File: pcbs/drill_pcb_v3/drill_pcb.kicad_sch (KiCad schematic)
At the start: 44 parts, among them J1 24V IN, J10 LIMIT SWITCH BOTTOM, J11 DEEP WEIGHT SENSOR, J12 SURFACE WEIGHT SENSOR, J13 SERVO 1, J14 SERVO 2, J15 STEPPER STORAGE, J16 TEST PADS, J2 uC COMMUNICATION, J3 ENCODER VERTICAL DRIVE, J4 LIMIT SWITCH TOP, J5 HEIGHT SENSOR, J6 STEPPER VERTICAL DRIVE, J7 DC MOTOR 24 V, J8 DC MOTOR UART, J9 ENCODER STORAGE, Q3 SI2333-TP, U1 ESP32-DevKitC, U2 LM3940, U3 INA219BxD

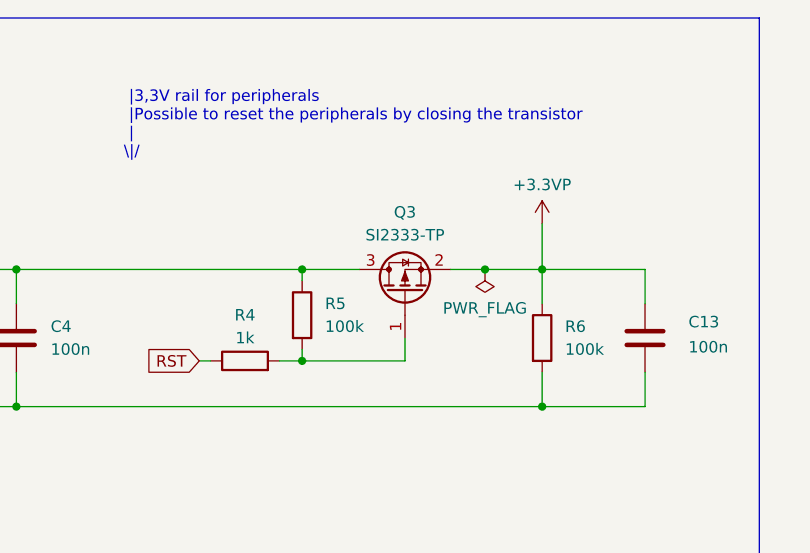
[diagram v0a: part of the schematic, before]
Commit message: Resolved mosfet misplacement for board v3. Deleted history.
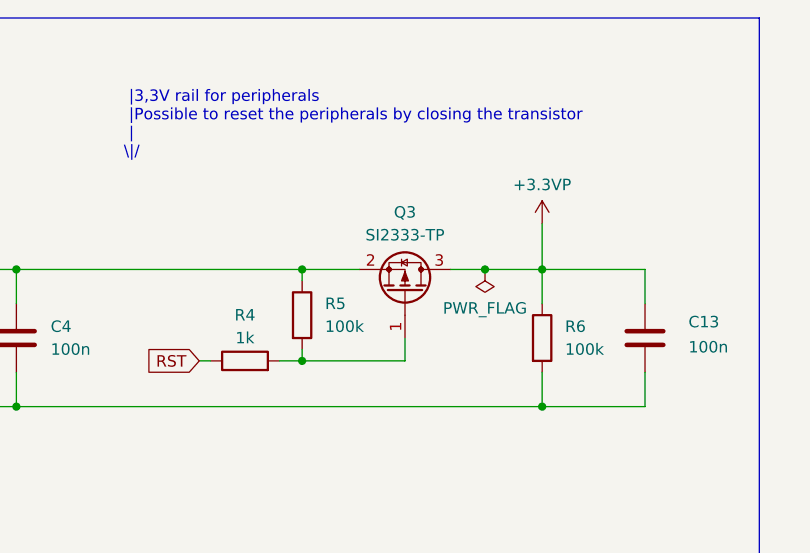
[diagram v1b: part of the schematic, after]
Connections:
- net +3.3V: now also Q3.2 (S); no longer Q3.3 (D)
- net +3.3VP: now also Q3.3 (D); no longer Q3.2 (S)
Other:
- moved on the sheet: Q3
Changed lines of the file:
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@@
 	)
 	(junction
-		(at 189.23 43.18)
-		(diameter 0)
-		(color 0 0 0 0)
-	)
-	(junction
 		(at 245.11 48.26)
 		(diameter 0)
@@
 	)
 	(junction
+		(at 189.23 43.18)
+		(diameter 0)
+		(color 0 0 0 0)
+	)
+	(junction
 		(at 231.14 116.84)
 		(diameter 0)
@@
 	)
 	(junction
-		(at 168.91 43.18)
+		(at 137.16 43.18)
 		(diameter 0)
 		(color 0 0 0 0)
 	)
 	(junction
-		(at 137.16 43.18)
+		(at 124.46 43.18)
 		(diameter 0)
 		(color 0 0 0 0)
 	)
 	(junction
-		(at 124.46 43.18)
+		(at 168.91 43.18)
 		(diameter 0)
 		(color 0 0 0 0)
@@
 	(symbol
 		(lib_id "Transistor_FET:Q_PMOS_GSD")
-		(at 180.34 45.72 90)
+		(at 180.34 45.72 270)
+		(mirror x)
 		(unit 1)
 		(body_style 1)
@@
 		(in_pos_files yes)
 		(dnp no)
-		(fields_autoplaced yes)
 		(property "Reference" "Q3"
 			(at 180.34 36.83 90)
@@
 		)
 		(property "Footprint" "Package_TO_SOT_SMD:SOT-23-3"
-			(at 177.8 40.64 0)
+			(at 182.88 40.64 0)
 			(hide yes)
 			(show_name no)

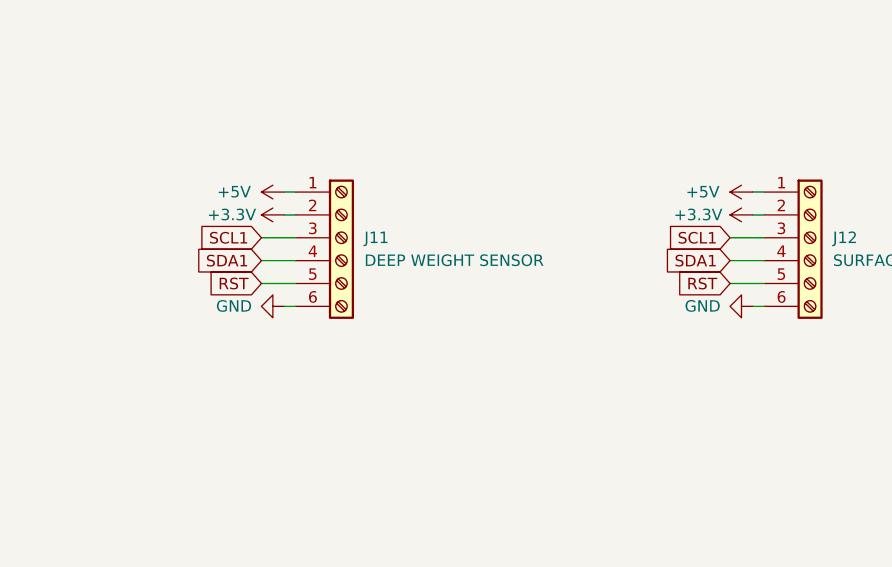
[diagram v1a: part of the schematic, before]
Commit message: ADC reset and Servo labels updated
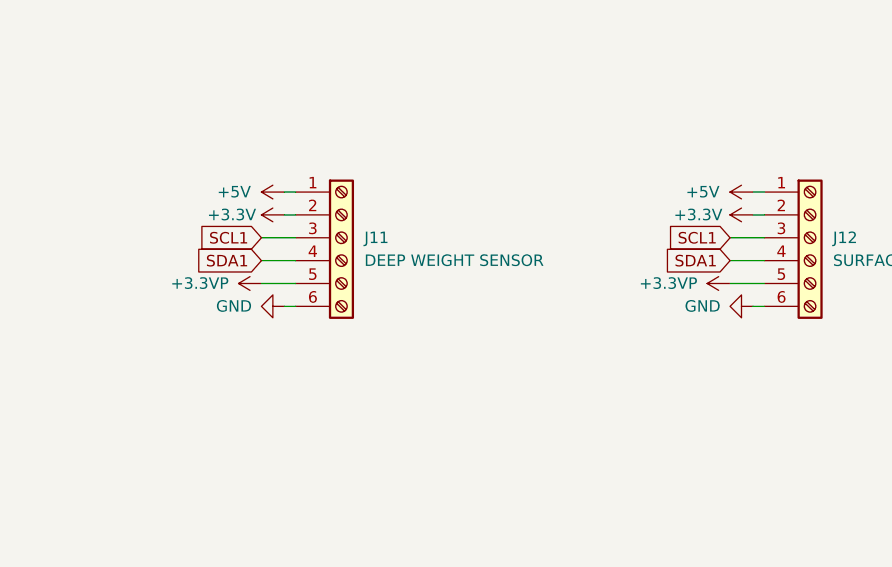
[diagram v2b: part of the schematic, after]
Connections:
- net +3.3VP: now also J11.5 (Pin_5), J12.5 (Pin_5)
- net RST: no longer J11.5 (Pin_5), J12.5 (Pin_5)
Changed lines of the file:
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@@
 		)
 	)
-	(global_label "RST"
-		(shape input)
-		(at 308.61 68.58 180)
-		(fields_autoplaced yes)
-		(effects
-			(font
-				(size 1.27 1.27)
-			)
-			(justify right)
-		)
-		(property "Intersheetrefs" "${INTERSHEET_REFS}"
-			(at 302.1777 68.58 0)
-			(hide yes)
-			(show_name no)
-			(do_not_autoplace no)
-			(effects
-				(font
-					(size 1.27 1.27)
-				)
-				(justify right)
-			)
-		)
-	)
 	(global_label "RX0"
 		(shape input)
@@
 		)
 	)
-	(global_label "RST"
-		(shape input)
-		(at 360.68 68.58 180)
-		(fields_autoplaced yes)
-		(effects
-			(font
-				(size 1.27 1.27)
-			)
-			(justify right)
-		)
-		(property "Intersheetrefs" "${INTERSHEET_REFS}"
-			(at 354.2477 68.58 0)
-			(hide yes)
-			(show_name no)
-			(do_not_autoplace no)
-			(effects
-				(font
-					(size 1.27 1.27)
-				)
-				(justify right)
-			)
-		)
-	)
 	(global_label "TX2"
 		(shape input)
@@
 	)
 	(symbol
+		(lib_id "power:+3.3VP")
+		(at 360.68 68.58 90)
+		(unit 1)
+		(body_style 1)
+		(exclude_from_sim no)
+		(in_bom yes)
+		(on_board yes)
+		(in_pos_files yes)
+		(dnp no)
+		(property "Reference" "#PWR045"
+			(at 361.95 64.77 0)
+			(hide yes)
+			(show_name no)
+			(do_not_autoplace no)
+			(effects
+				(font
+					(size 1.27 1.27)
+				)
+			)
+		)
+		(property "Value" "+3.3VP"
+			(at 353.822 68.58 90)
+			(show_name no)
+			(do_not_autoplace no)
+			(effects
+				(font
+					(size 1.27 1.27)
+				)
+			)
+		)
+		(property "Footprint" ""
+			(at 360.68 68.58 0)
+			(hide yes)
+			(show_name no)
+			(do_not_autoplace no)
+			(effects
+				(font
+					(size 1.27 1.27)
+				)
+			)
+		)
+		(property "Datasheet" ""
+			(at 360.68 68.58 0)
+			(hide yes)
+			(show_name no)
+			(do_not_autoplace no)
+			(effects
+				(font
+					(size 1.27 1.27)
+				)
+			)
+		)
+		(property "Description" "Power symbol creates a global label with name \"+3.3VP\""
+			(at 360.68 68.58 0)
+			(hide yes)
+			(show_name no)
+			(do_not_autoplace no)
+			(effects
+				(font
+					(size 1.27 1.27)
+				)
+			)
+		)
+		(pin "1"
+		)
+		(instances
+			(project "drill_pcb"
+				(path "/bebf97b1-2f7f-4d03-a427-fe976f4b2313"
+					(reference "#PWR045")
+					(unit 1)
+				)
+			)
+		)
+	)
+	(symbol
 		(lib_id "Device:R")
 		(at 168.91 48.26 0)
@@
 					(unit 1)
 				)
+			)
+		)
+	)
+	(symbol
+		(lib_id "power:+3.3VP")
+		(at 308.61 68.58 90)
+		(unit 1)
+		(body_style 1)
+		(exclude_from_sim no)
+		(in_bom yes)
+		(on_board yes)
+		(in_pos_files yes)
+		(dnp no)
+		(property "Reference" "#PWR044"
+			(at 309.88 64.77 0)
+			(hide yes)
+			(show_name no)
+			(do_not_autoplace no)
+			(effects
+				(font
+					(size 1.27 1.27)
+				)
+			)
+		)
+		(property "Value" "+3.3VP"
+			(at 301.752 68.58 90)
+			(show_name no)
+			(do_not_autoplace no)
+			(effects
+				(font
+					(size 1.27 1.27)
+				)
+			)
+		)
+		(property "Footprint" ""
+			(at 308.61 68.58 0)
+			(hide yes)
+			(show_name no)
+			(do_not_autoplace no)
+			(effects
+				(font
+					(size 1.27 1.27)
+				)
+			)
+		)
+		(property "Datasheet" ""
+			(at 308.61 68.58 0)
+			(hide yes)
+			(show_name no)
+			(do_not_autoplace no)
+			(effects
+				(font
+					(size 1.27 1.27)
+				)
+			)
+		)
+		(property "Description" "Power symbol creates a global label with name \"+3.3VP\""
+			(at 308.61 68.58 0)
+			(hide yes)
+			(show_name no)
+			(do_not_autoplace no)
+			(effects
+				(font
+					(size 1.27 1.27)
+				)
+			)
+		)
+		(pin "1"
+		)
+		(instances
+			(project "drill_pcb"
+				(path "/bebf97b1-2f7f-4d03-a427-fe976f4b2313"
+					(reference "#PWR044")
+					(unit 1)
+				)
